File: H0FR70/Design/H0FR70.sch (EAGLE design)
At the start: 38 parts, among them P2 HEXABIT_17.32_NO_P6_P7_P12, Q1 BSS123, Q2 STD36P4LLF6, U2 INA199A2DCKT, X1 XTALL_CSTCE8M00G52

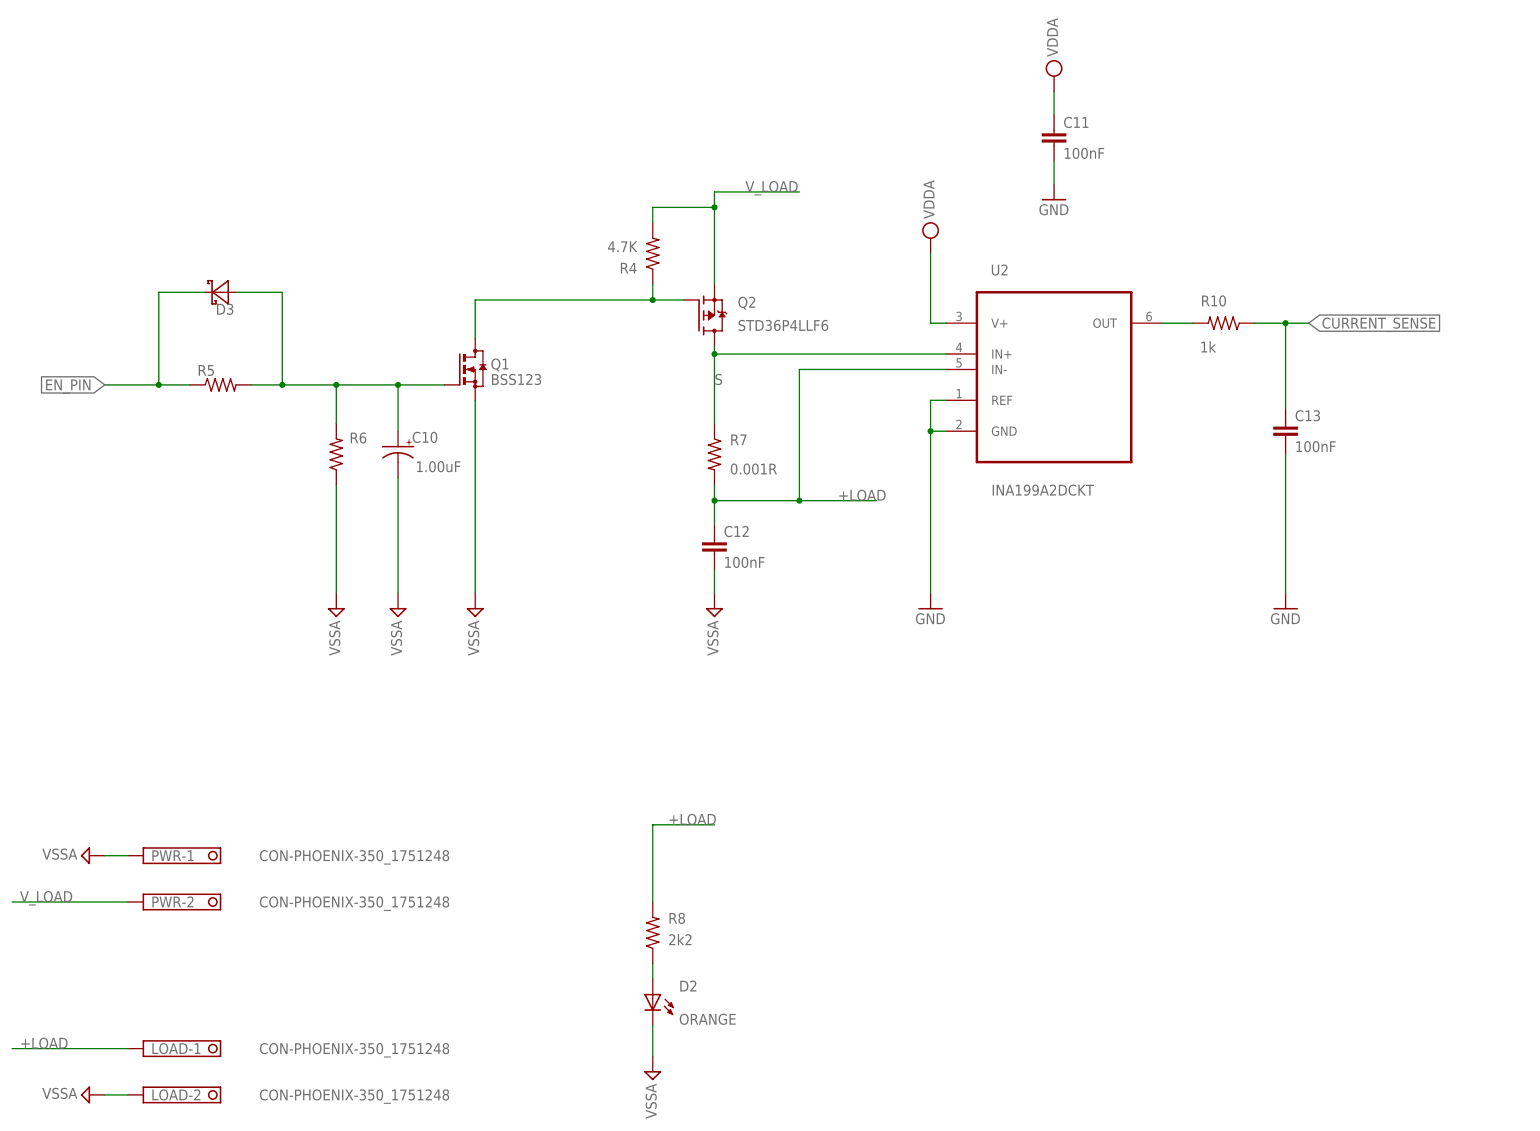
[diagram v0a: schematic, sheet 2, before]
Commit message: changing power connector to PTR500 (AK500/3) adding voltage diveder at the gate of power transistor (4.7/14.7)
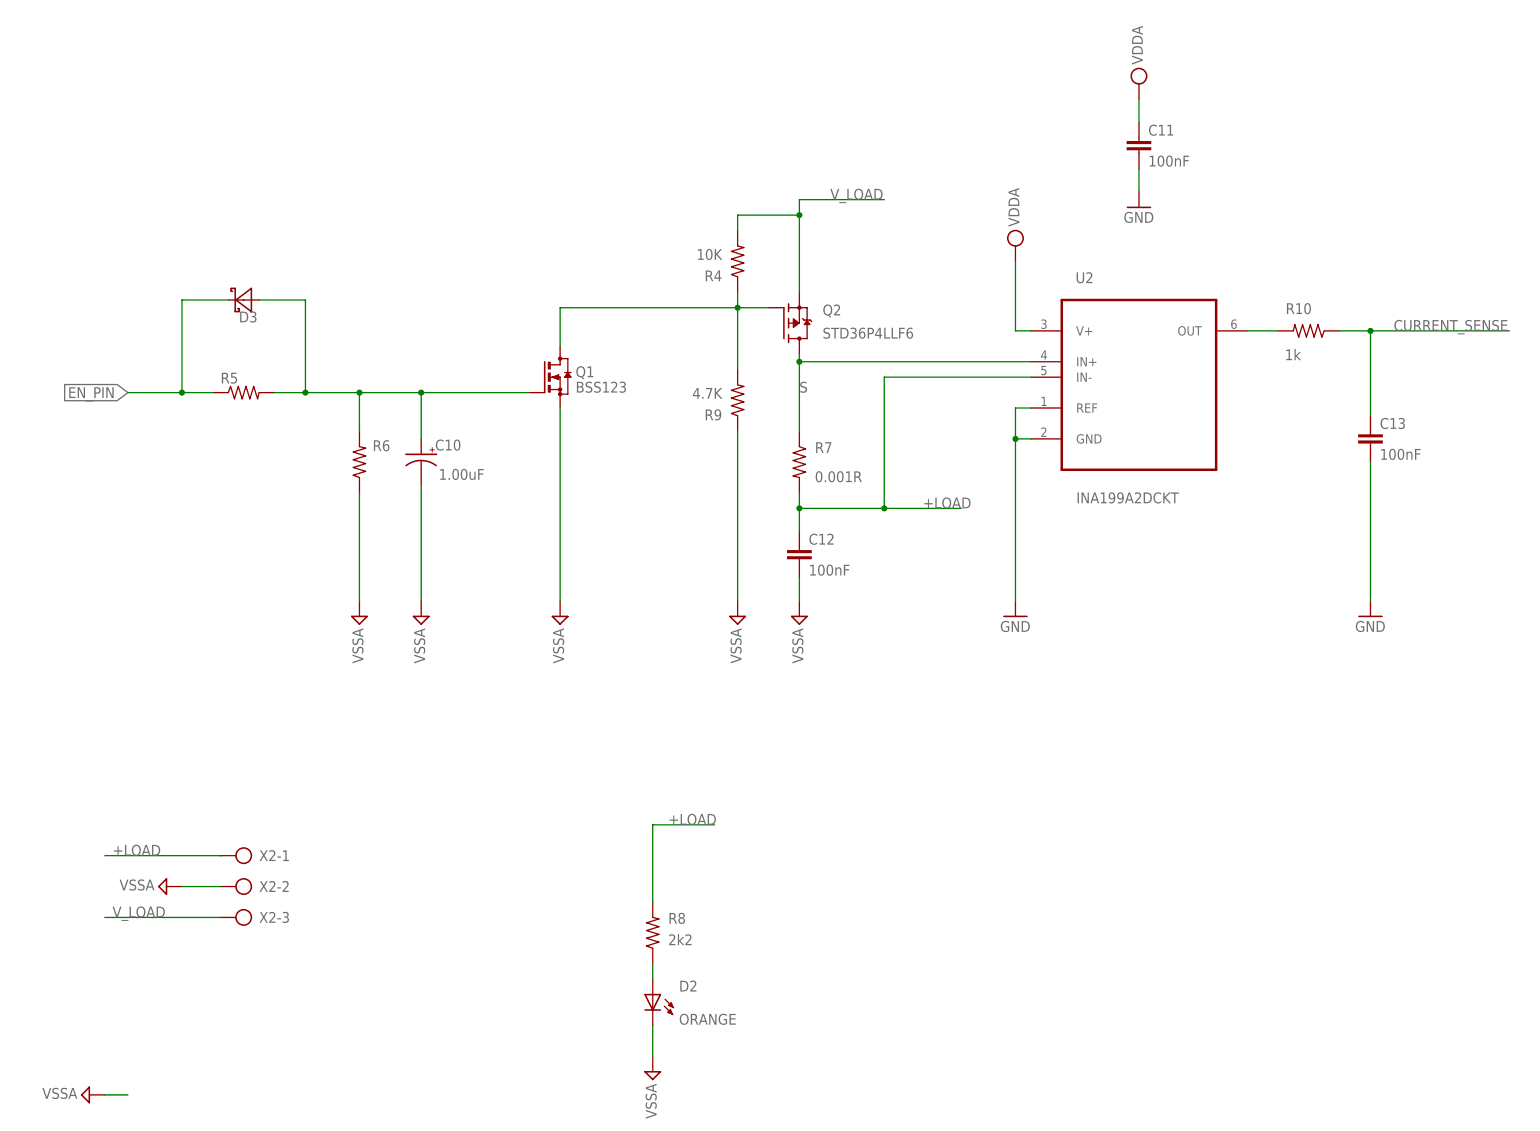
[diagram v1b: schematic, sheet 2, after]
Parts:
- removed LOAD, PWR: CON-PHOENIX-350_1751248, Hexabitz:CON-PHOENIX-350_1751248
- added R9: 4.7K, Hexabitz:R-0603
- added X2: (no value), con-ptr500:AK500/3
- R4: value 4.7K -> 10K
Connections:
- net +LOAD: now also X2-1.KL; no longer LOAD-1.K
- net AGND: now also R9.1, X2-2.KL; no longer LOAD-2.K, PWR-1.K
- net N$7: now also R9.2
- net V_LOAD: now also X2-3.KL; no longer PWR-2.K
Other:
- moved on the sheet: C10, C11, C12, C13, D3, Q1, Q2, R10, R4, R5, R6, R7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

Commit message: adding: zenar at gate + 0R res
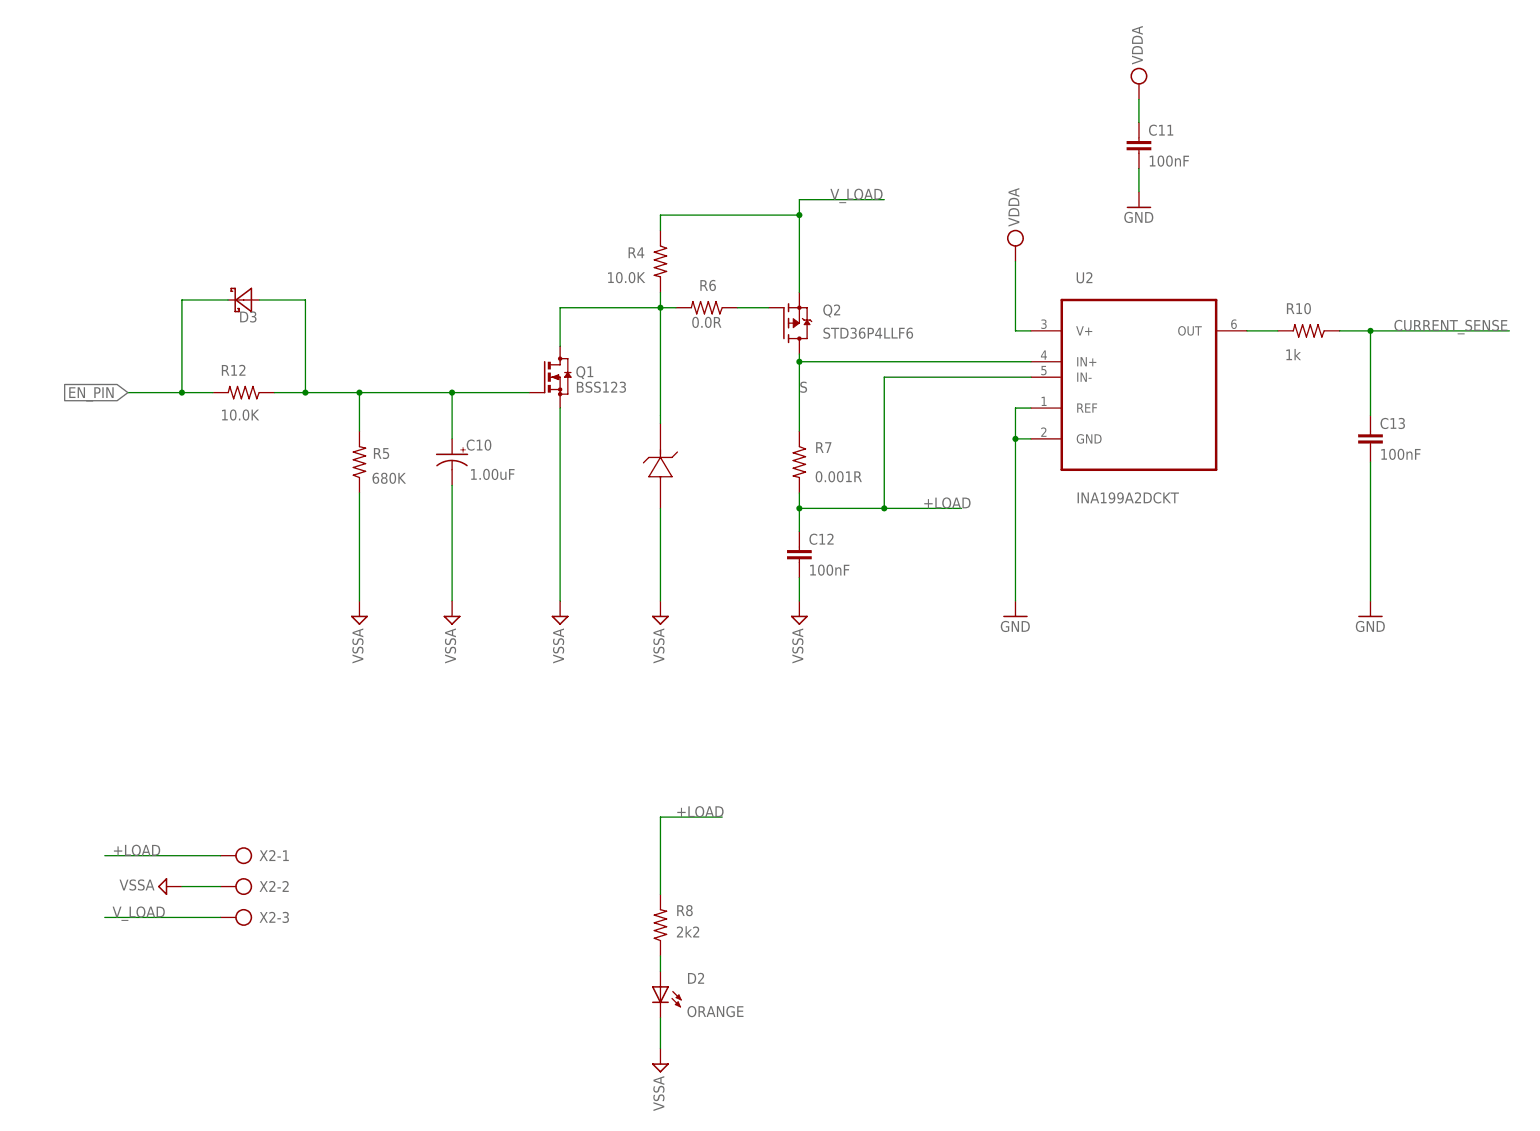
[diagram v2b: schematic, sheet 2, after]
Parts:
- removed R9: 4.7K, Hexabitz:R-0603
- added D4: BZT52C2V0S-7-F, Hexabitz:BZT52C2V0S-7-F
- added R12: 10.0K, Hexabitz:R-0603
- R10: MFN (none) -> Yageo; MPN (none) -> RC0603JR-071KL; OCTOPART_URL (none) -> https://octopart.com/rc0603jr-071kl-yageo-55402888?r=sp; RESISTANCE (none) -> 1k; TOLERANCE (none) -> 5%
- R4: value 10K -> 10.0K; MFN (none) -> Yageo; MPN (none) -> RC0603JR-0710KL; OCTOPART_URL (none) -> https://octopart.com/search?q=RC0603JR-0710KL&start=0; RESISTANCE (none) -> 10.0K Ohm; TOLERANCE (none) -> 5%
- R5: value (none) -> 680K; MFN (none) -> Yageo; MPN (none) -> RC0603JR-07680KL; OCTOPART_URL (none) -> https://octopart.com/rc0603jr-07680kl-yageo-40953169?r=sp; RESISTANCE (none) -> 680K Ohm; TOLERANCE (none) -> 5%
- R6: value (none) -> 0.0R; MFN (none) -> Yageo; MPN (none) -> RC0603JR-070RL; OCTOPART_URL (none) -> https://octopart.com/rc0603jr-070rl-yageo-1241539?r=sp&s=X2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; RESISTANCE (none) -> 0.0 Ohm
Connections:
- new net N$10: Q2.G, R6.1
- net AGND: now also D4.1, R5.1; no longer R6.1, R9.1
- net EN_PIN: now also R12.2; no longer R5.1
- net N$13: now also R12.1; no longer R6.2
- net N$7: now also D4.2, R4.2, R6.2; no longer Q2.G, R4.1, R9.2
- net V_LOAD: now also R4.1; no longer R4.2
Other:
- note added: "Gain = 100 V/V"
- note added: "Power and Load Connector"
- note added: "SPST MOSFET Switch 20A 40V"
- note removed: "SPST MOSFET Switch upto 20A 40V"
- note removed: "load_connector"
- note removed: "power_connector"
- moved on the sheet: C10, D2, R4, R5, R6, R8
